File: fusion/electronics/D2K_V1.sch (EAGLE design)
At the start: 5 parts, among them M1 Active Cooler SC1148, U1 Raspberry Pi 5

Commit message: Wire the controls and the audio: schematic sheets 2 and 3
- Library: ESP32-S3-Zero (castellated rows, solder pads, USB-C), 6x6 tact
  switch, New 3DS XL Circle Pad (pinout to verify), Waveshare WM8960 Audio
  Board (header pinout from its schematic) and the 2030 speaker.
- D2K_V1 now has three sheets. Sheet 2: ESP32-S3-Zero on USB to the Pi's
  second USB 2.0 port (W7), 15 buttons to GND on internal pull-ups, both
  Circle Pads on ADC1 GPIO1-4, with GPIO10, 40-42 and 43/44 kept free for
  battery, Hall, vibration, power control and a UART link. Sheet 3: WM8960
  on the Pi's I2C1 and I2S pins (W8, pins 1/3/5/9/12/35/38/40, labelled on
  sheet 1) and the two speakers on its bridged outputs (W9).
- wiring.md gets the pin tables and new warnings (3.3 V-only ESP32, Circle
  Pad pinout, WM8960 amplifier on the Pi 3V3 rail, speaker plug mismatch).
- The flat-cable model goes back to the plain route: the hinge crossing is
  a side note in constraints.md, behind a switch in script 75.

Co-Authored-By: Claude Opus 5.5 <noreply@anthropic.com>
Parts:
- added JS1: Circle Pad LEFT (move), D2K:CIRCLE_PAD_N3DSXL
- added JS2: Circle Pad RIGHT (C-stick), D2K:CIRCLE_PAD_N3DSXL
- added LS1: Speaker LEFT, D2K:SPEAKER_8R_2W
- added LS2: Speaker RIGHT, D2K:SPEAKER_8R_2W
- added SW1: BTN_DPAD_UP, D2K:TACT_SWITCH_6X6
- added SW10: BTN_SELECT, D2K:TACT_SWITCH_6X6
- added SW11: BTN_HOME, D2K:TACT_SWITCH_6X6
- added SW12: BTN_L1, D2K:TACT_SWITCH_6X6
- added SW13: BTN_R1, D2K:TACT_SWITCH_6X6
- added SW14: BTN_L2, D2K:TACT_SWITCH_6X6
- added SW15: BTN_R2, D2K:TACT_SWITCH_6X6
- added SW2: BTN_DPAD_DOWN, D2K:TACT_SWITCH_6X6
- added SW3: BTN_DPAD_LEFT, D2K:TACT_SWITCH_6X6
- added SW4: BTN_DPAD_RIGHT, D2K:TACT_SWITCH_6X6
- added SW5: BTN_A, D2K:TACT_SWITCH_6X6
- added SW6: BTN_B, D2K:TACT_SWITCH_6X6
- added SW7: BTN_X, D2K:TACT_SWITCH_6X6
- added SW8: BTN_Y, D2K:TACT_SWITCH_6X6
- added SW9: BTN_START, D2K:TACT_SWITCH_6X6
- added U2: ESP32-S3-Zero - USB HID, D2K:ESP32_S3_ZERO
- added U3: WM8960 Audio Board, D2K:WM8960_AUDIO_BOARD
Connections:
- new net BTN_A: SW5.P1, U2MAIN.GPIO9
- new net BTN_B: SW6.P1, U2MAIN.GPIO11
- new net BTN_DPAD_DOWN: SW2.P1, U2MAIN.GPIO6
- new net BTN_DPAD_LEFT: SW3.P1, U2MAIN.GPIO7
- new net BTN_DPAD_RIGHT: SW4.P1, U2MAIN.GPIO8
- new net BTN_DPAD_UP: SW1.P1, U2MAIN.GPIO5
- new net BTN_HOME: SW11.P1, U2PADS.GPIO16
- new net BTN_L1: SW12.P1, U2PADS.GPIO17
- new net BTN_L2: SW14.P1, U2PADS.GPIO38
- new net BTN_R1: SW13.P1, U2PADS.GPIO18
- new net BTN_R2: SW15.P1, U2PADS.GPIO39
- new net BTN_SELECT: SW10.P1, U2PADS.GPIO15
- new net BTN_START: SW9.P1, U2PADS.GPIO14
- new net BTN_X: SW7.P1, U2MAIN.GPIO12
- new net BTN_Y: SW8.P1, U2MAIN.GPIO13
- new net ESP_3V3: JS1.VCC, JS2.VCC, U2MAIN.3V3_OUT
- new net I2C1_SCL: U1GPIO.GPIO3_SCL1, U3HDR.SCL
- new net I2C1_SDA: U1GPIO.GPIO2_SDA1, U3HDR.SDA
- new net I2S_BCLK: U1GPIO.GPIO18_PCM_CLK, U3HDR.CLK@10, U3HDR.CLK@9
- new net I2S_DIN: U1GPIO.GPIO20_PCM_DIN, U3HDR.RXSDA_ADC_OUT
- new net I2S_DOUT: U1GPIO.GPIO21_PCM_DOUT, U3HDR.TXSDA_DAC_IN
- new net I2S_LRCLK: U1GPIO.GPIO19_PCM_FS, U3HDR.WS@11, U3HDR.WS@12
- new net LSTICK_X: JS1.X, U2MAIN.GPIO1
- new net LSTICK_Y: JS1.Y, U2MAIN.GPIO2
- new net RSTICK_X: JS2.X, U2MAIN.GPIO3
- new net RSTICK_Y: JS2.Y, U2MAIN.GPIO4
- new net SPK_LN: LS1.SPK-, U3SPK.LN
- new net SPK_LP: LS1.SPK+, U3SPK.LP
- new net SPK_RN: LS2.SPK-, U3SPK.RN
- new net SPK_RP: LS2.SPK+, U3SPK.RP
- new net USB2_1_D+: U1USB2_1.D+, U2USB.D+
- new net USB2_1_D-: U1USB2_1.D-, U2USB.D-
- new net USB2_1_VBUS: U1USB2_1.VBUS, U2USB.VBUS
- net 3V3: now also U1GPIO.3V3@1, U3HDR.VCC@1, U3HDR.VCC@2
- net GND: now also JS1.GND, JS2.GND, SW1.P2, SW10.P2, SW11.P2, SW12.P2, SW13.P2, SW14.P2, SW15.P2, SW2.P2, SW3.P2, SW4.P2, SW5.P2, SW6.P2, SW7.P2, SW8.P2, SW9.P2, U1GPIO.GND@2, U1USB2_1.GND, U2MAIN.GND@1, U2USB.GND, U3HDR.GND@1, U3HDR.GND@2
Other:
- note added: "! Circle Pad pinout NOT verified: measure VCC/GND/X/Y before wiring. Feed 3.3 V (ESP_3V3), never 5 V."
- note added: "15 buttons active-low to GND (internal pull-ups), 2 Circle Pads on ADC1, USB to the Pi"
- note added: "6x6 tact switch: pins 1-2 and 3-4 are joined inside - wire diagonally (1 to GPIO, 4 to GND)."
- note added: "= USB-C VBUS on board"
- note added: "D2K V1 - 1/3 Pi 5 and screens"
- note added: "D2K V1 - 2/3 Controls (ESP32-S3-Zero USB HID)"
- note added: "D2K V1 - 3/3 Audio (WM8960 + 2 speakers)"
- note added: "ESP32 is 3.3 V only (not 5 V tolerant). GPIO3 (RSTICK_X) is a strapping pin: fine as analog input."
- note added: "Face buttons, D-pad (6x6 tact on the breadboard)"
- note added: "Header pins 5/7 = SCL/SDA per the schematic netlist: check the board silkscreen before wiring."
- note added: "Header pins L1-L9 / R1-R9 sit on the breadboard; GPIO14-18, 38, 39 are solder pads (F front, B back)."
- note added: "Headset (HDMI audio, until the WM8960 works)"
- note added: "Kept free: GPIO10 (ADC battery), GPIO40-42 (Hall, vibration, Pi power), GPIO43/44 (UART to Pi)."
- note added: "Labelled pins 1, 3, 5, 9, 12, 35, 38, 40: WM8960 audio board (sheet 3), W8 jumper wires."
- note added: "Linux: WM8960 overlay (dtoverlay=wm8960-soundcard, to confirm on the Pi); codec I2C address 0x1A."
- note added: "Pi 5 I2S (GPIO18-21) + I2C1 (GPIO2/3) -> Waveshare WM8960 Audio Board -> two 8 ohm 2 W speakers"
- note added: "Speakers go in the upper half: 4 wires through the hinge, power/audio side (fusion/constraints.md)."
- note added: "Start/Select/Home, shoulders"
- note added: "The board runs from the Pi 3V3 rail, including its speaker amplifier (SPKVDD): ~0.4 W/ch max, measure the current."
- note added: "Unused: Pi HDMI1, DISP0, USB3, Ethernet; 5in DC micro-USB, VGA, speaker header. Pi USB2_1: ESP32 (sheet 2)."
- note added: "W7 USB-A -> USB-C DATA cable: HID gamepad + ESP32 power"
- note added: "W8 8 jumper wires from the Pi GPIO header (sheet 1): 3V3 pin 1, SDA 3, SCL 5, GND 9, BCLK 12, LRCLK 35, DIN 38, DOUT 40"
- note added: "W9 speaker leads (PH1.25 plugs: need a 4-pin adapter / recrimp)"
- note added: "avoid: strapping pin"
- note added: "free: ADC1 for battery voltage"
- note added: "free: Pi power control"
- note added: "free: UART to Pi (later)"
- note added: "free: lid Hall sensor"
- note added: "free: vibration PWM"
- note added: "open"
- note added: "open: MCLK = on-board 24 MHz"
- note removed: "D2K V1 - bench interconnect"
- note removed: "Headset (V1 sound = HDMI audio)"
- note removed: "Unused: Pi HDMI1, DISP0, USB2_1, USB3, Ethernet; 5in DC micro-USB, VGA, speaker header."

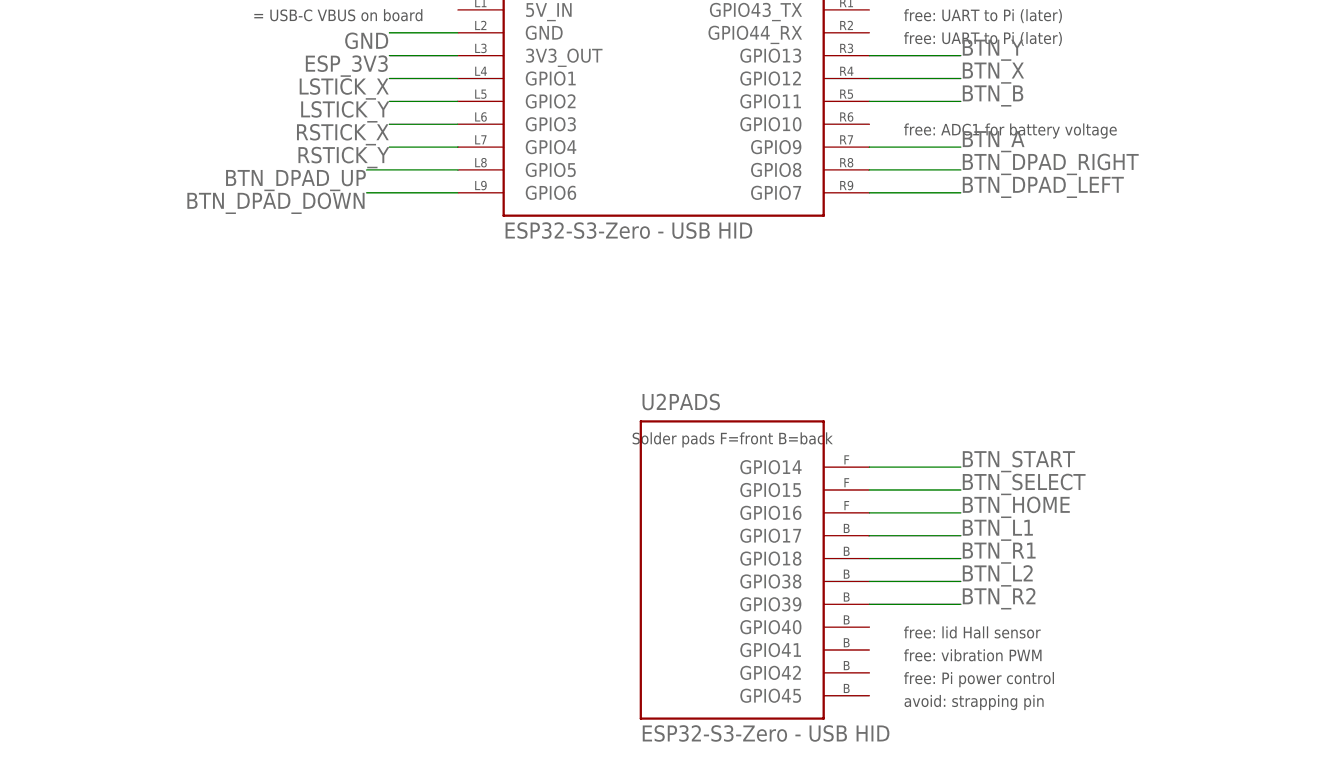
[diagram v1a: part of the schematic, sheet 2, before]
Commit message: Add the bench wiring page: breadboard view and Pi GPIO jumpers
electronics/gen_breadboard.py generates breadboard_v1.html from the
D2K_V1 pin plan: a 2D MB-102 view with the ESP32-S3-Zero across the
channel, the 15 tact switches in four groups, both Circle Pads and every
jumper routed in its own lane with its hole coordinates, plus the Pi GPIO
header jumpers to the WM8960 board and the 4in screen lead, each with a
tickable wire list. The generator asserts that no two button wires cross;
to make that possible L2/R2 moved to GPIO6/GPIO5 and the D-pad up/down,
Start, Select, Home, L1, R1 to the solder pads, and the schematic follows
the same table.

Co-Authored-By: Claude Opus 5.5 <noreply@anthropic.com>
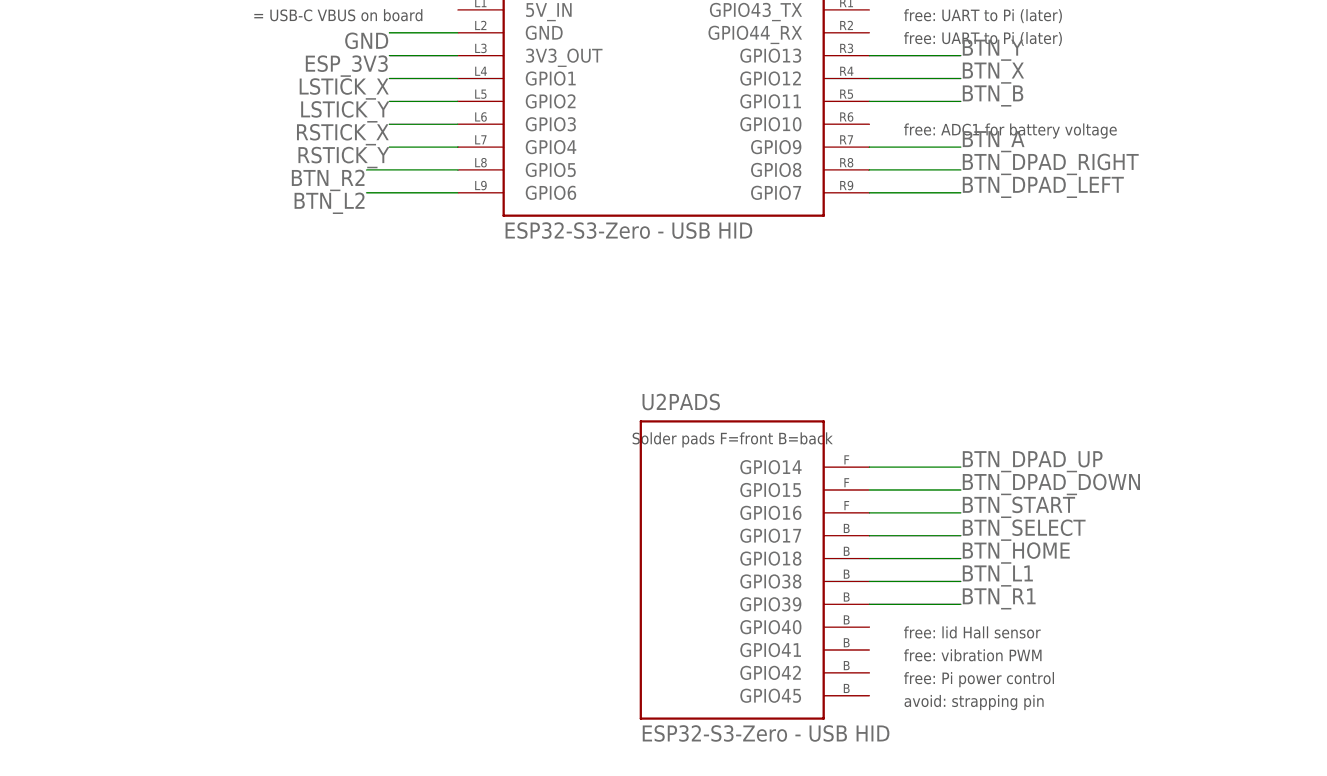
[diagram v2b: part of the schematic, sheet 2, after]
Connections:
- net BTN_DPAD_DOWN: now also U2PADS.GPIO15; no longer U2MAIN.GPIO6
- net BTN_DPAD_UP: now also U2PADS.GPIO14; no longer U2MAIN.GPIO5
- net BTN_HOME: now also U2PADS.GPIO18; no longer U2PADS.GPIO16
- net BTN_L1: now also U2PADS.GPIO38; no longer U2PADS.GPIO17
- net BTN_L2: now also U2MAIN.GPIO6; no longer U2PADS.GPIO38
- net BTN_R1: now also U2PADS.GPIO39; no longer U2PADS.GPIO18
- net BTN_R2: now also U2MAIN.GPIO5; no longer U2PADS.GPIO39
- net BTN_SELECT: now also U2PADS.GPIO17; no longer U2PADS.GPIO15
- net BTN_START: now also U2PADS.GPIO16; no longer U2PADS.GPIO14
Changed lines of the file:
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@@
 <net name="BTN_DPAD_UP" class="0">
 <segment>
-<pinref part="U2" gate="MAIN" pin="GPIO5"/>
-<wire x1="-5.08" y1="-20.32" x2="-15.24" y2="-20.32" width="0.1524" layer="91"/>
-<label x="-15.24" y="-20.32" size="1.778" layer="95" rot="R180"/>
+<pinref part="U2" gate="PADS" pin="GPIO14"/>
+<wire x1="40.64" y1="-53.34" x2="50.8" y2="-53.34" width="0.1524" layer="91"/>
+<label x="50.8" y="-53.34" size="1.778" layer="95"/>
 </segment>
 <segment>
@@
 <net name="BTN_DPAD_DOWN" class="0">
 <segment>
-<pinref part="U2" gate="MAIN" pin="GPIO6"/>
-<wire x1="-5.08" y1="-22.86" x2="-15.24" y2="-22.86" width="0.1524" layer="91"/>
-<label x="-15.24" y="-22.86" size="1.778" layer="95" rot="R180"/>
+<pinref part="U2" gate="PADS" pin="GPIO15"/>
+<wire x1="40.64" y1="-55.88" x2="50.8" y2="-55.88" width="0.1524" layer="91"/>
+<label x="50.8" y="-55.88" size="1.778" layer="95"/>
 </segment>
 <segment>
@@
 <net name="BTN_START" class="0">
 <segment>
-<pinref part="U2" gate="PADS" pin="GPIO14"/>
-<wire x1="40.64" y1="-53.34" x2="50.8" y2="-53.34" width="0.1524" layer="91"/>
-<label x="50.8" y="-53.34" size="1.778" layer="95"/>
+<pinref part="U2" gate="PADS" pin="GPIO16"/>
+<wire x1="40.64" y1="-58.42" x2="50.8" y2="-58.42" width="0.1524" layer="91"/>
+<label x="50.8" y="-58.42" size="1.778" layer="95"/>
 </segment>
 <segment>
@@
 <net name="BTN_SELECT" class="0">
 <segment>
-<pinref part="U2" gate="PADS" pin="GPIO15"/>
-<wire x1="40.64" y1="-55.88" x2="50.8" y2="-55.88" width="0.1524" layer="91"/>
-<label x="50.8" y="-55.88" size="1.778" layer="95"/>
+<pinref part="U2" gate="PADS" pin="GPIO17"/>
+<wire x1="40.64" y1="-60.96" x2="50.8" y2="-60.96" width="0.1524" layer="91"/>
+<label x="50.8" y="-60.96" size="1.778" layer="95"/>
 </segment>
 <segment>
@@
 <net name="BTN_HOME" class="0">
 <segment>
-<pinref part="U2" gate="PADS" pin="GPIO16"/>
-<wire x1="40.64" y1="-58.42" x2="50.8" y2="-58.42" width="0.1524" layer="91"/>
-<label x="50.8" y="-58.42" size="1.778" layer="95"/>
+<pinref part="U2" gate="PADS" pin="GPIO18"/>
+<wire x1="40.64" y1="-63.5" x2="50.8" y2="-63.5" width="0.1524" layer="91"/>
+<label x="50.8" y="-63.5" size="1.778" layer="95"/>
 </segment>
 <segment>
@@
 <net name="BTN_L1" class="0">
 <segment>
-<pinref part="U2" gate="PADS" pin="GPIO17"/>
-<wire x1="40.64" y1="-60.96" x2="50.8" y2="-60.96" width="0.1524" layer="91"/>
-<label x="50.8" y="-60.96" size="1.778" layer="95"/>
+<pinref part="U2" gate="PADS" pin="GPIO38"/>
+<wire x1="40.64" y1="-66.04" x2="50.8" y2="-66.04" width="0.1524" layer="91"/>
+<label x="50.8" y="-66.04" size="1.778" layer="95"/>
 </segment>
 <segment>
@@
 <net name="BTN_R1" class="0">
 <segment>
-<pinref part="U2" gate="PADS" pin="GPIO18"/>
-<wire x1="40.64" y1="-63.5" x2="50.8" y2="-63.5" width="0.1524" layer="91"/>
-<label x="50.8" y="-63.5" size="1.778" layer="95"/>
+<pinref part="U2" gate="PADS" pin="GPIO39"/>
+<wire x1="40.64" y1="-68.58" x2="50.8" y2="-68.58" width="0.1524" layer="91"/>
+<label x="50.8" y="-68.58" size="1.778" layer="95"/>
 </segment>
 <segment>
@@
 <net name="BTN_L2" class="0">
 <segment>
-<pinref part="U2" gate="PADS" pin="GPIO38"/>
-<wire x1="40.64" y1="-66.04" x2="50.8" y2="-66.04" width="0.1524" layer="91"/>
-<label x="50.8" y="-66.04" size="1.778" layer="95"/>
+<pinref part="U2" gate="MAIN" pin="GPIO6"/>
+<wire x1="-5.08" y1="-22.86" x2="-15.24" y2="-22.86" width="0.1524" layer="91"/>
+<label x="-15.24" y="-22.86" size="1.778" layer="95" rot="R180"/>
 </segment>
 <segment>
@@
 <net name="BTN_R2" class="0">
 <segment>
-<pinref part="U2" gate="PADS" pin="GPIO39"/>
-<wire x1="40.64" y1="-68.58" x2="50.8" y2="-68.58" width="0.1524" layer="91"/>
-<label x="50.8" y="-68.58" size="1.778" layer="95"/>
+<pinref part="U2" gate="MAIN" pin="GPIO5"/>
+<wire x1="-5.08" y1="-20.32" x2="-15.24" y2="-20.32" width="0.1524" layer="91"/>
+<label x="-15.24" y="-20.32" size="1.778" layer="95" rot="R180"/>
 </segment>
 <segment>
